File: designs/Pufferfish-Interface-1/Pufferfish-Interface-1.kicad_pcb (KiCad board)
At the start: 2 copper layers, 51 parts, among them Q1 DMN10H220L, Q2 DMN10H220L, Q3 DMN10H220L, Q4 2SC1815, Q5 2N7002E, Q6 2N7002E, Q7 2N7002E, SW1 SW_SPST_LED, SW2 SW_SPST_LED, SW3 SW_SPST_LED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

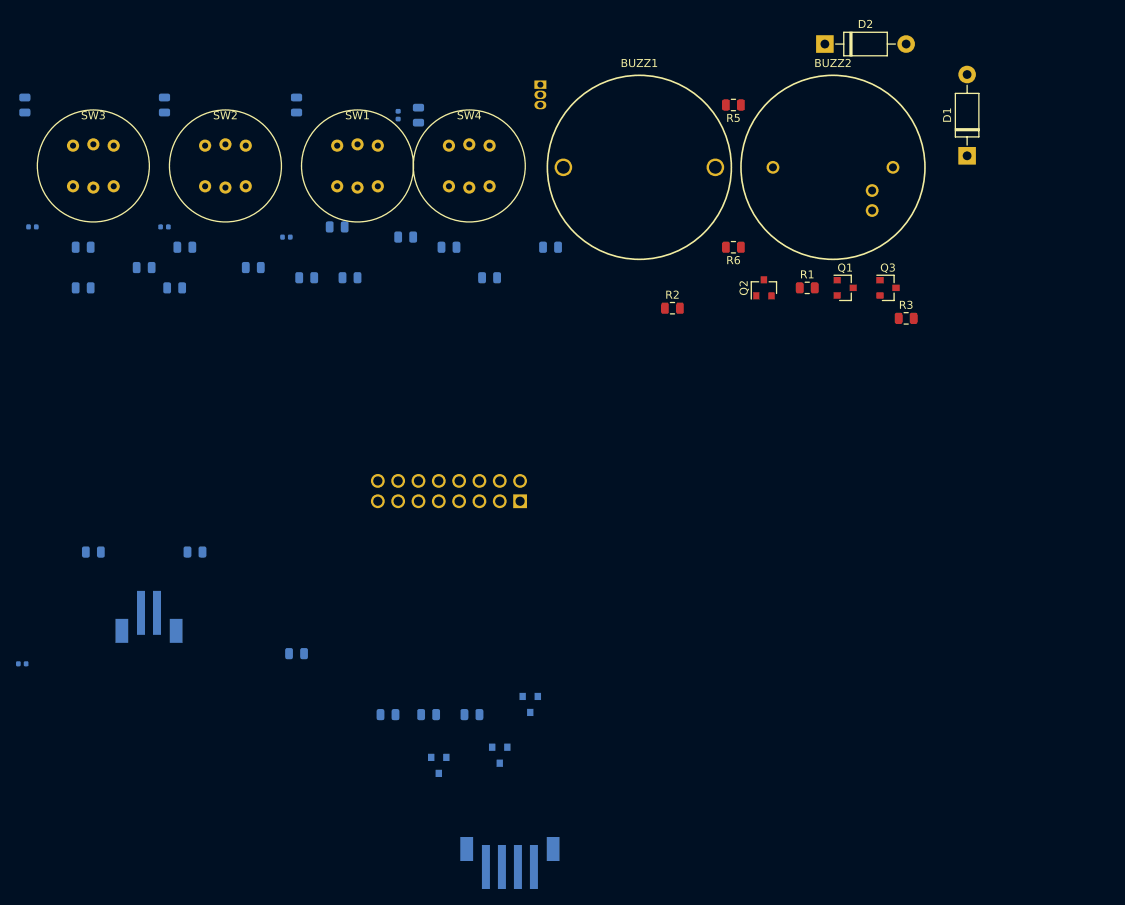
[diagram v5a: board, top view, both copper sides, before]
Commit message: first board layout part placement
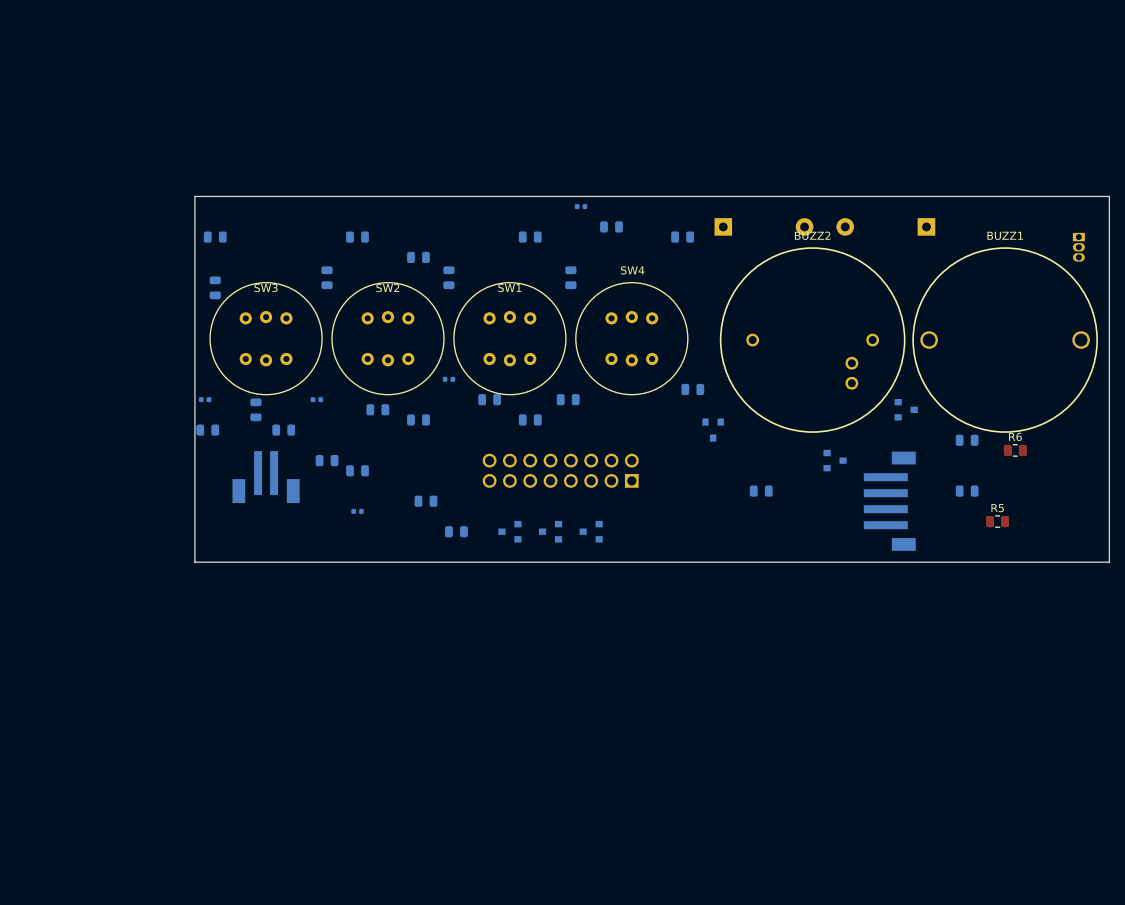
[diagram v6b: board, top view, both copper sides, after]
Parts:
- D1, D2, Q1, Q2, Q3, R1, R2, R3: moved to B.Cu
- moved Q4 70.0 mm to (129.5, 20.3)
- moved CONN1 65.6 mm to (105.4, 53.3), turned to 90 degrees
- moved R5 61.7 mm to (119.4, 55.9), turned to 0 degrees
- moved R4 57.4 mm to (115.6, 45.7)
- moved BUZZ1 50.6 mm to (120.3, 33.2)
- moved D5 46.0 mm to (39.4, 54.6)
- moved R8 45.7 mm to (89.8, 52.1)
- moved R6 43.4 mm to (121.6, 47.0), turned to 0 degrees
- moved R1 38.4 mm to (61.0, 43.2)
- moved R11 36.3 mm to (47.0, 43.2)
- moved C3 34.5 mm to (39.4, 49.5)
- moved C4 33.0 mm to (21.6, 26.7)
- moved Q7 32.4 mm to (63.5, 57.1), turned to 180 degrees
- moved D1 31.7 mm to (85.1, 19.1), turned to 0 degrees
- moved R22 30.7 mm to (30.1, 44.5)
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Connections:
- R1 pad 2: Net-(R1-Pad2) -> GND
- R10 pad 1: 3.3V -> 5V
- R11 pad 1: 3.3V -> 5V
- R18 pad 1: 3.3V -> 5V
- R19 pad 1: 3.3V -> 5V
- R2 pad 2: Net-(R2-Pad2) -> GND
- R3 pad 2: Net-(R3-Pad2) -> GND
- R7 pad 2: Net-(R7-Pad2) -> GND
- R8 pad 2: Net-(R8-Pad2) -> GND
- R9 pad 2: Net-(R9-Pad2) -> GND
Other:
- board outline added: 114.3 x 45.7 mm

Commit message: pdf
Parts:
- moved R16 3.16 mm to (22.5, 47.0)
- moved CONN1 2.54 mm to (105.4, 50.8)
- moved CONN3 1.80 mm to (29.2, 51.1)
- moved C3 1.27 mm to (39.4, 48.3)
- moved C4 1.27 mm to (21.6, 25.4)
- moved D3 1.27 mm to (50.8, 36.8)
- moved D4 1.27 mm to (34.3, 39.4)
- moved Q2 1.27 mm to (83.8, 43.2)
- moved R1 1.27 mm to (61.0, 41.9)
- moved R10 1.27 mm to (55.9, 39.4)
- moved R11 1.27 mm to (47.0, 41.9)
- moved R19 1.27 mm to (65.7, 39.4)
- moved R22 1.27 mm to (30.1, 43.2)
- moved R3 1.27 mm to (115.6, 50.8)
- moved R5 1.27 mm to (119.4, 54.6)
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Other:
- board size 114.3 x 45.7 mm -> 114.3 x 43.2 mm

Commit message: first compete layout
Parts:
- R5, R6: moved to B.Cu
- moved R5 8.44 mm to (127.8, 55.6)
- moved R6 7.21 mm to (128.8, 46.2)
- moved R4 4.60 mm to (119.8, 46.2)
- moved BUZZ2 3.55 mm to (92.7, 31.9)
- moved D7 2.50 mm to (65.6, 18.3)
- moved R3 2.05 mm to (117.6, 51.1)
- moved R23 1.70 mm to (70.4, 19.3)
- moved Q5 1.48 mm to (57.1, 55.1)
- moved Q7 1.48 mm to (62.2, 55.1)
- moved Q6 1.48 mm to (67.3, 55.1)
- moved C5 1.27 mm to (64.8, 24.1)
- moved D1 1.27 mm to (83.8, 17.8)
- moved R21 1.27 mm to (78.7, 19.1)
- moved R8 1.27 mm to (88.6, 50.8)
- moved C2 1.27 mm to (34.3, 24.1)
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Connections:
- CONN1 pad 1: 5V -> +12V
- CONN2 pad 2: 5V -> +12V
- R5 pad 1: 5V -> +12V
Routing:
- net 3.3V: track 0.00 -> 133.1 mm, vias 0 -> 3
- net 5V: track 0.00 -> 101.1 mm, vias 0 -> 6
- net ALARM2_CNTRL: track 0.00 -> 65.9 mm, vias 0 -> 2
- net +12V: track 0.00 -> 63.9 mm, vias 0 -> 2
- net GND: track 0.00 -> 61.0 mm, vias 0 -> 10
- net ALARM1_LOW: track 0.00 -> 60.4 mm, vias 0 -> 2
- net SET_EXTRA1: track 0.00 -> 54.9 mm
- net Net-(CONN1-Pad2): track 0.00 -> 53.7 mm
- net Net-(CONN1-Pad4): track 0.00 -> 48.8 mm, vias 0 -> 2
- net ALARM1_HIGH: track 0.00 -> 43.2 mm
- net Net-(BUZZ2-Pad3): track 0.00 -> 42.2 mm
- net Net-(CONN1-Pad3): track 0.00 -> 41.9 mm
- net Net-(BUZZ1-Pad1): track 0.00 -> 40.8 mm
- net SET_LOCK: track 0.00 -> 40.4 mm
- net Net-(R12-Pad2): track 0.00 -> 38.9 mm
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- added copper zone on B.Cu, net GND
- added copper zone on F.Cu, net GND
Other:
- net class Thick added: clearance 0.2, trace_width 0.508, via_dia 0.8, via_drill 0.4
